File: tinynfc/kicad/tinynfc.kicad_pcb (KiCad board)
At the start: 2 copper layers, 40 x 40 mm, 15 parts, among them Q1 Diodes_DFN1006-3, U1 NXP_SOT902-3_XQFN8, U2 VQFN-20-1EP_3x3mm_P0.4mm_EP1.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

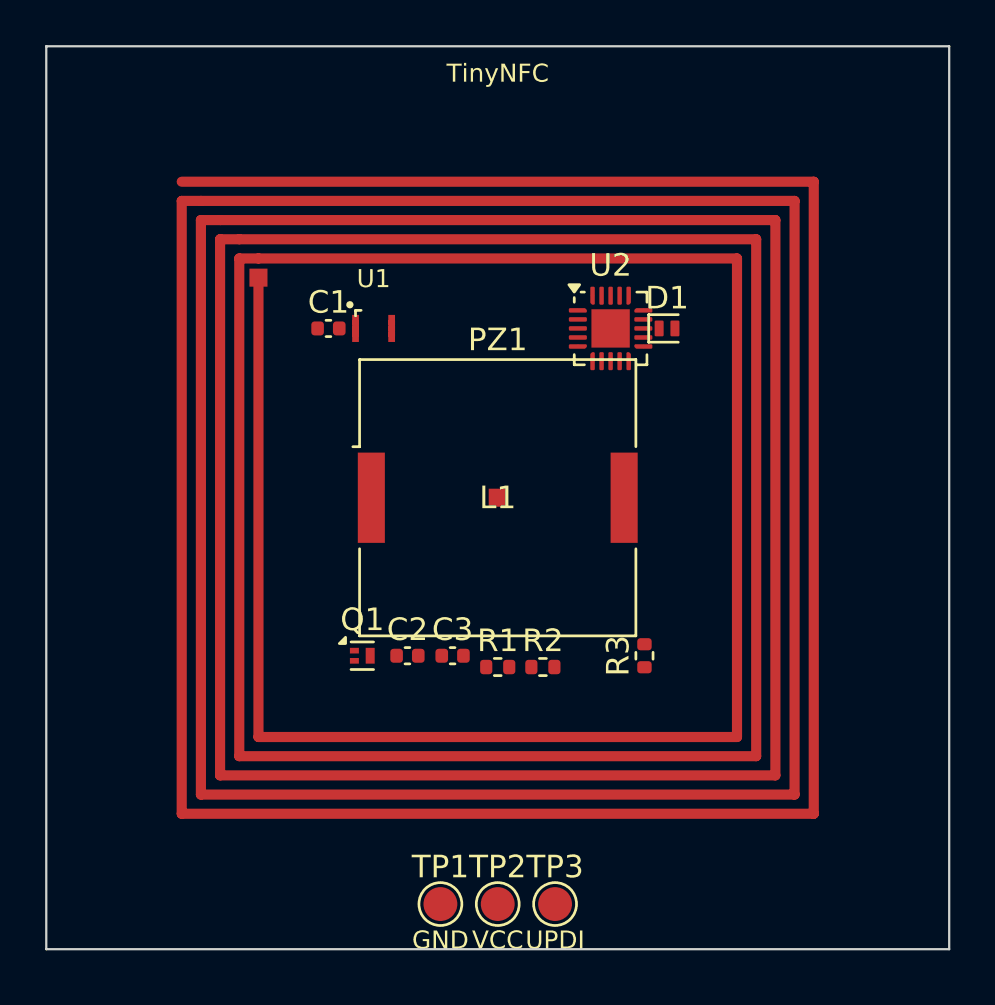
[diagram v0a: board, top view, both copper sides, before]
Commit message: Shrink TinyNFC to 28 mm postage stamp, not card size
Drop the outline from 40 mm to 28 mm with a 23 mm / 6-turn spiral, switch
to a 9×9 FUET-9018 piezo so the island fits, hide footprint silk refs that
were landing on copper, and refresh BOM/design costs for the smaller board.

Co-authored-by: Jason Hall <imjasonh@users.noreply.github.com>
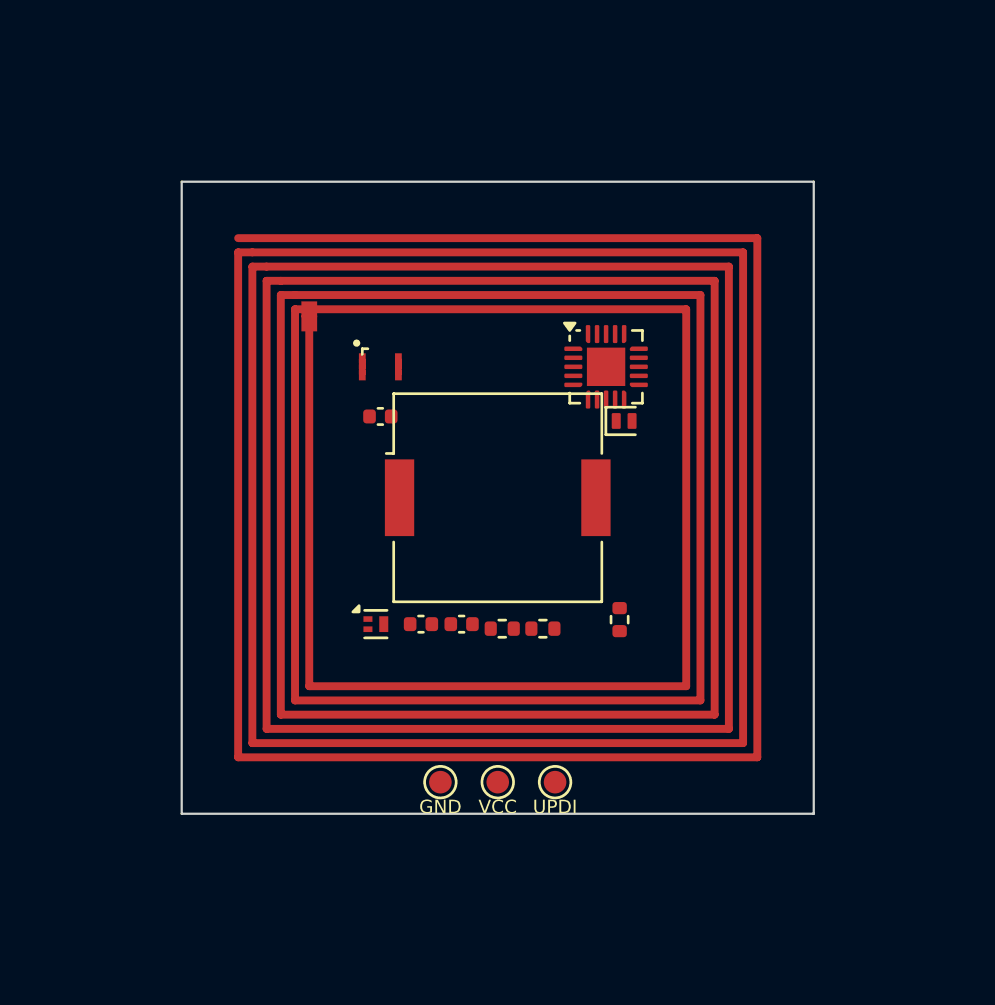
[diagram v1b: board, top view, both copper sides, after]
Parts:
- PZ1: value Buzzer_Murata_PKLCS1212E -> Buzzer_Murata_PKMCS0909E; footprint Buzzer_Murata_PKLCS1212E -> Buzzer_Murata_PKMCS0909E
- TP1, TP2, TP3: value TestPoint_Pad_D1.5mm -> TestPoint_Pad_D1.0mm; footprint TestPoint_Pad_D1.5mm -> TestPoint_Pad_D1.0mm
- moved TP1 5.40 mm to (-2.54, 12.6)
- moved TP2 5.40 mm to (0.00, 12.6)
- moved TP3 5.40 mm to (2.54, 12.6)
- moved C1 4.53 mm to (-5.20, -3.60)
- moved D1 4.52 mm to (5.60, -3.40)
- moved R3 1.94 mm to (5.40, 5.40)
- moved U1 1.73 mm to (-5.20, -5.80)
- moved R1 1.71 mm to (0.20, 5.80)
- moved U2 1.71 mm to (4.80, -5.80)
- moved R2 1.70 mm to (2.00, 5.80)
- moved C2 1.52 mm to (-3.40, 5.60)
- moved Q1 1.52 mm to (-5.40, 5.60)
- moved C3 1.46 mm to (-1.60, 5.60)
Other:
- board size 40 x 40 mm -> 28 x 28 mm
- board text removed: "TinyNFC"

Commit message: Add BOM qty breaks and US-quarter scale on TinyNFC PCB
Price 10 / 50 / 100 assembled runs in BOM.md, document 1.6 mm FR-4
(~3.4 mm assembled) thickness, and draw a Dwgs.User quarter outline
beside the 28 mm board for scale.

Co-authored-by: Jason Hall <imjasonh@users.noreply.github.com>
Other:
- board text added: "US quarter"
- board text added: "assembled ~3.4 mm tall"
- board text added: "board 28×28×1.6 mm"
- board text added: "Ø24.26 mm"

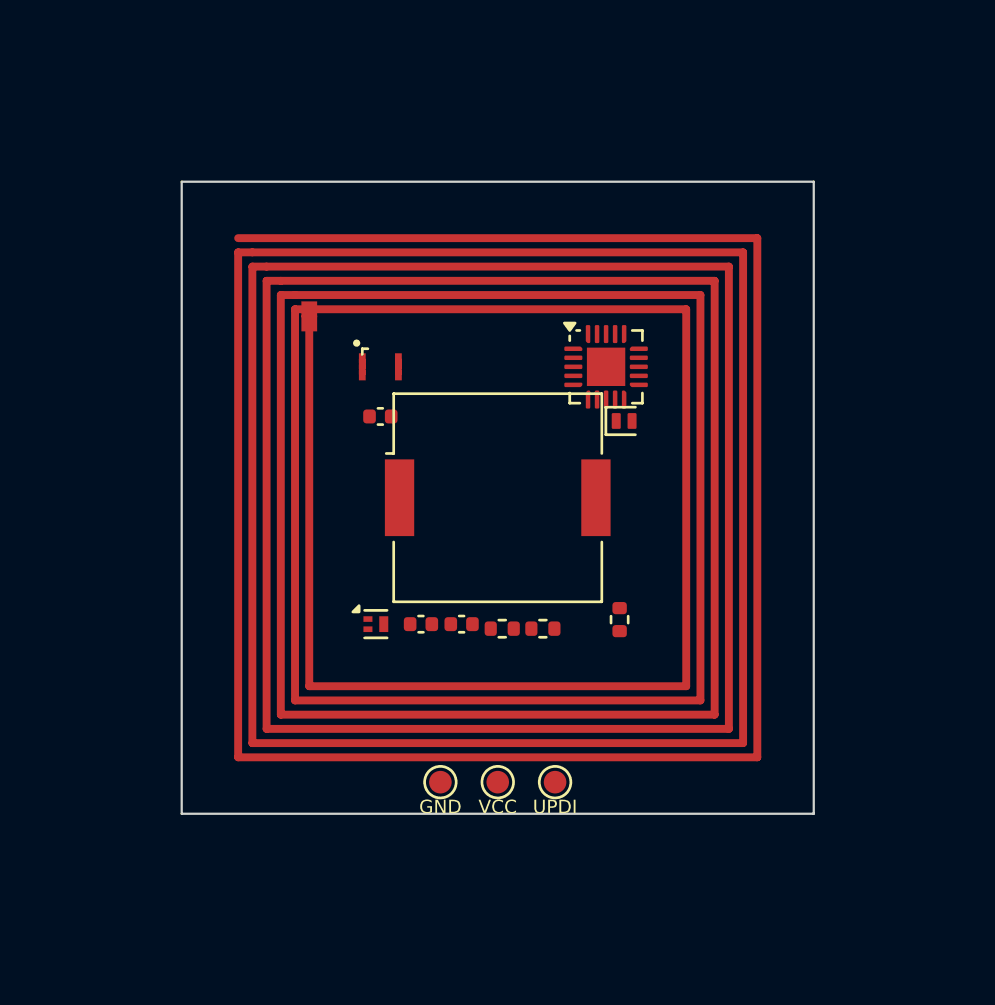
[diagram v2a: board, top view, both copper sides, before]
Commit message: Make TinyNFC board and antenna circular
Switch the Edge.Cuts outline to Ø 28 mm and replace the square spiral with
a Ø 24 mm Archimedean spiral so the coil matches phone NFC geometry better.
Update design, BOM, and README for the round postage-stamp disc.

Co-authored-by: Jason Hall <imjasonh@users.noreply.github.com>
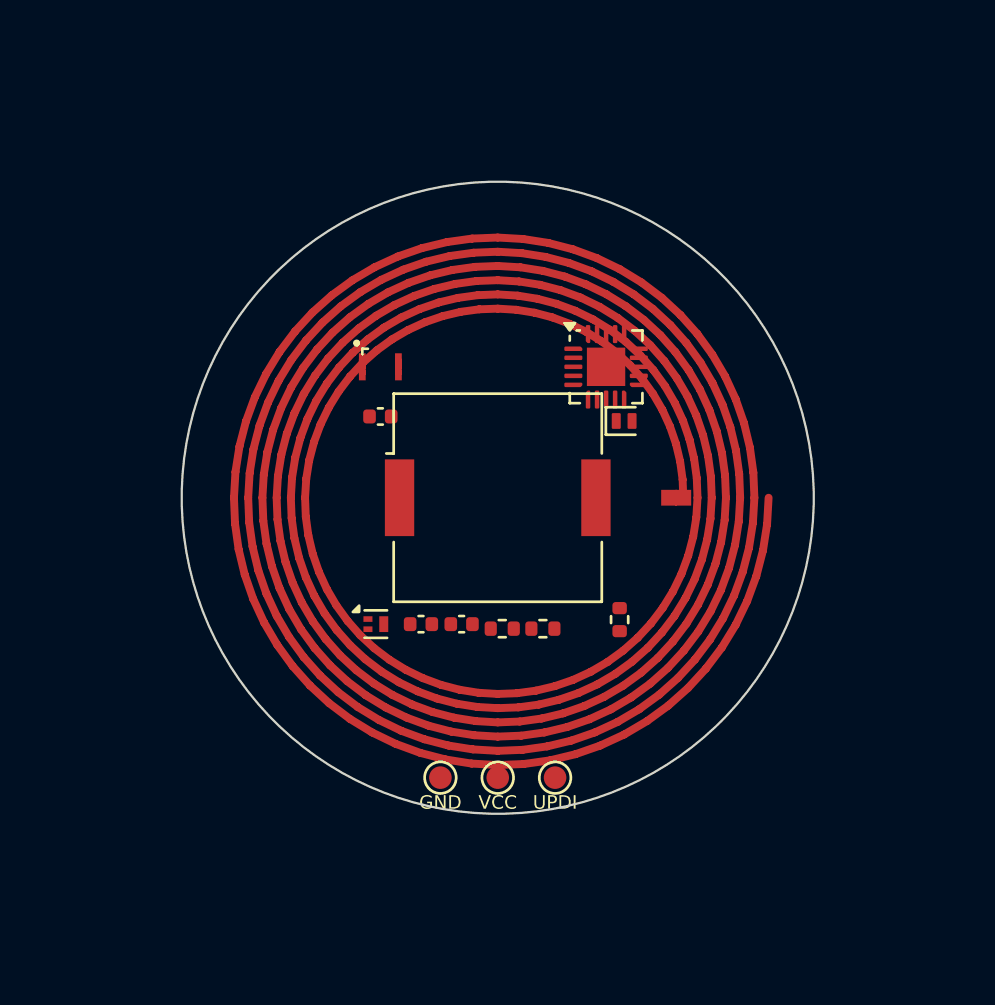
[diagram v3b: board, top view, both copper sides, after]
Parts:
- L1: value PCB_Antenna_RectSpiral -> PCB_Antenna_RoundSpiral; footprint PCB_Antenna_RectSpiral -> PCB_Antenna_RoundSpiral
- moved TP1 0.20 mm to (-2.54, 12.4)
- moved TP2 0.20 mm to (0.00, 12.4)
- moved TP3 0.20 mm to (2.54, 12.4)
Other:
- outline, holes or cut-outs redrawn
- board text added: "board Ø28×1.6 mm"
- board text removed: "board 28×28×1.6 mm"

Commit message: Keep TinyNFC parts clear of the circular spiral
Shift the piezo north and pack the ATtiny, NT3H, passives, and UPDI
pads into the south island. Stop the spiral at an inner clear radius,
move feeds to the west rim, and fail generation on pad/antenna or
pad/pad overlaps.

Co-authored-by: Jason Hall <imjasonh@users.noreply.github.com>
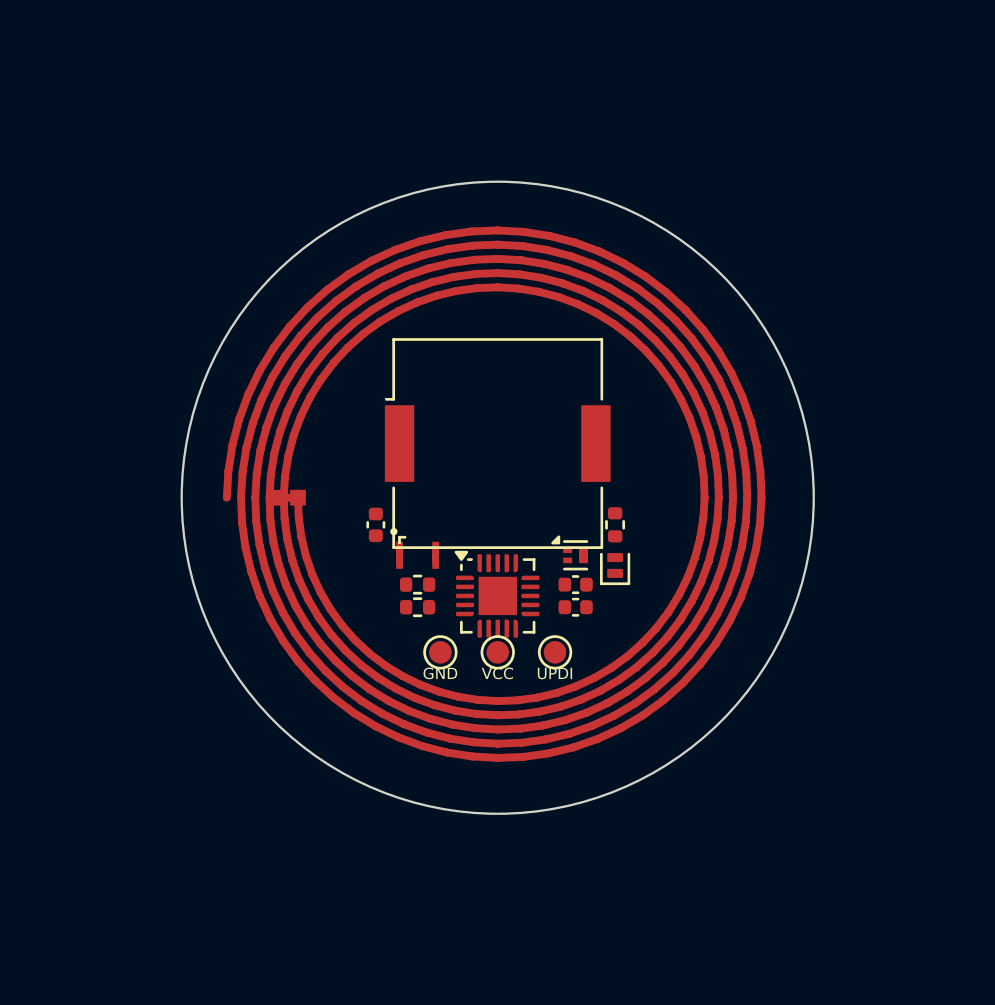
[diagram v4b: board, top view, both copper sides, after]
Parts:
- moved U2 11.2 mm to (0.00, 4.35)
- moved Q1 9.36 mm to (3.45, 2.55)
- moved U1 8.51 mm to (-3.55, 2.55)
- moved C2 7.07 mm to (3.45, 3.85)
- moved D1 6.41 mm to (5.20, 3.00), turned to 90 degrees
- moved R2 5.63 mm to (-3.55, 4.85)
- moved TP1 5.55 mm to (-2.54, 6.85)
- moved TP2 5.55 mm to (0.00, 6.85)
- moved TP3 5.55 mm to (2.54, 6.85)
- moved C3 5.11 mm to (3.45, 4.85)
- moved C1 4.80 mm to (-5.40, 1.20), turned to 90 degrees
- moved R1 4.23 mm to (-3.55, 3.85)
- moved R3 4.20 mm to (5.20, 1.20)
- moved PZ1 2.40 mm to (0.00, -2.40)

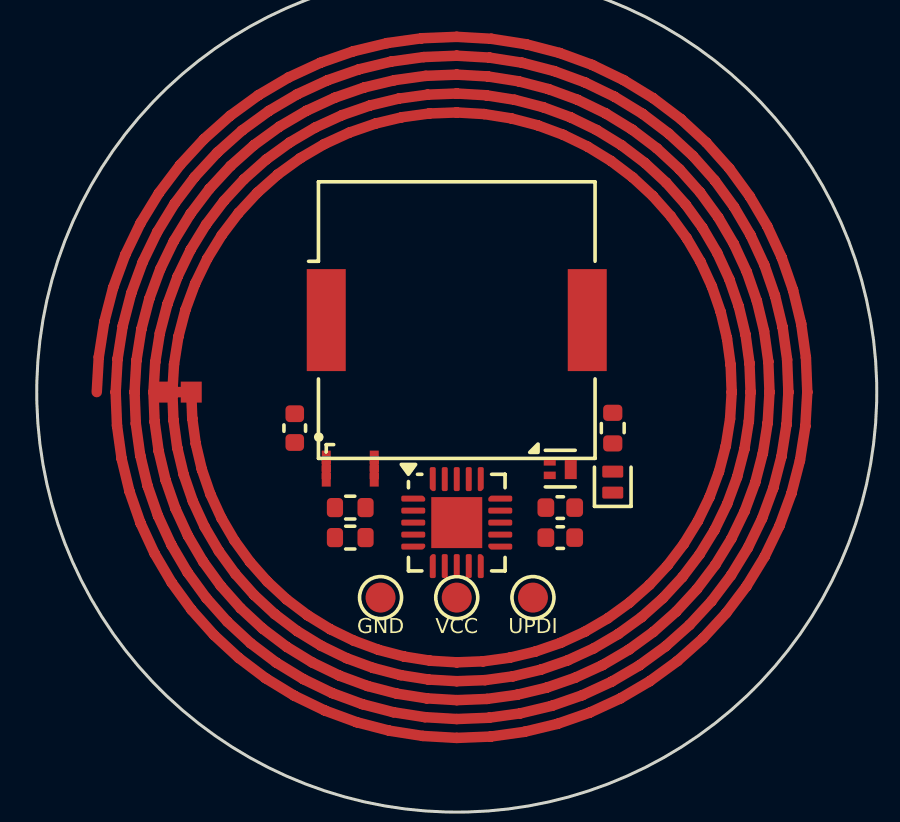
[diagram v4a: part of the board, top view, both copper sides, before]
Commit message: Spread TinyNFC parts into piezo east/west flanks
Put the antenna tune and VOUT bypass caps in the NW/NE pockets beside
the piezo, keep the NT3H and power chain on the side columns, and leave
the ATtiny plus UPDI pads on the south rim.

Co-authored-by: Jason Hall <imjasonh@users.noreply.github.com>
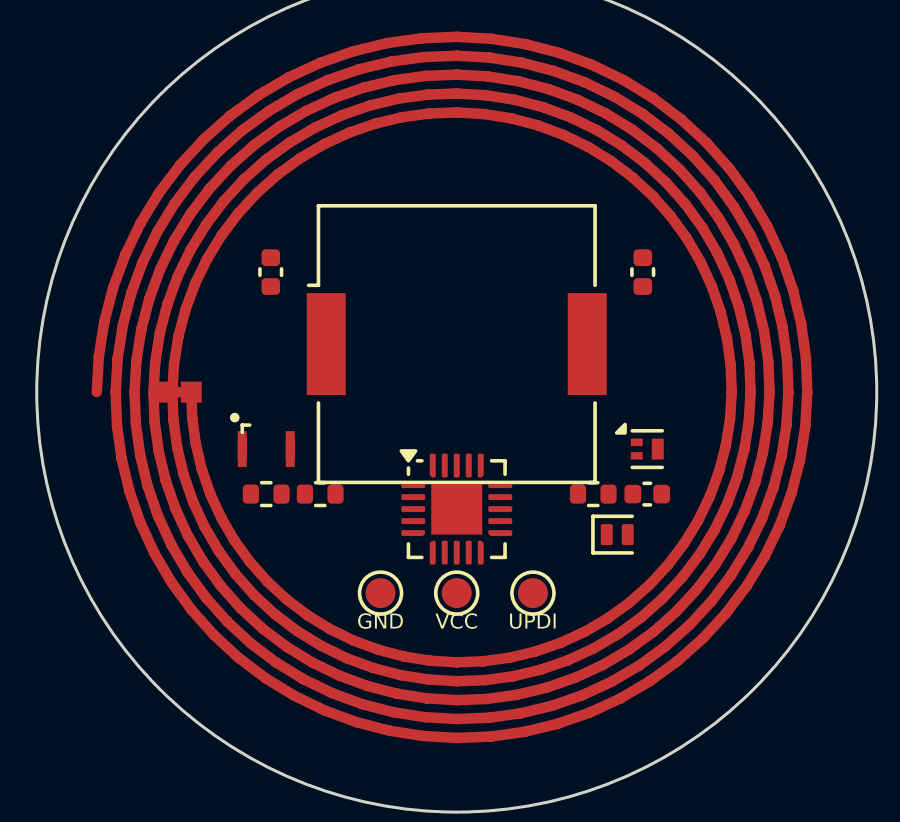
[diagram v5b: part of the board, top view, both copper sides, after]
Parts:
- moved C2 8.32 mm to (6.20, -4.00), turned to 90 degrees
- moved C1 5.26 mm to (-6.20, -4.00)
- moved C3 3.24 mm to (6.35, 3.40)
- moved Q1 2.97 mm to (6.35, 1.90)
- moved U1 2.87 mm to (-6.35, 1.90)
- moved R1 2.84 mm to (-6.35, 3.40)
- moved R3 2.29 mm to (4.55, 3.40), turned to 0 degrees
- moved R2 1.76 mm to (-4.55, 3.40)
- moved D1 1.76 mm to (5.35, 4.75), turned to 0 degrees
- moved PZ1 0.80 mm to (0.00, -1.60)
- moved U2 0.45 mm to (0.00, 3.90)
- moved TP1 0.15 mm to (-2.54, 6.70)
- moved TP2 0.15 mm to (0.00, 6.70)
- moved TP3 0.15 mm to (2.54, 6.70)

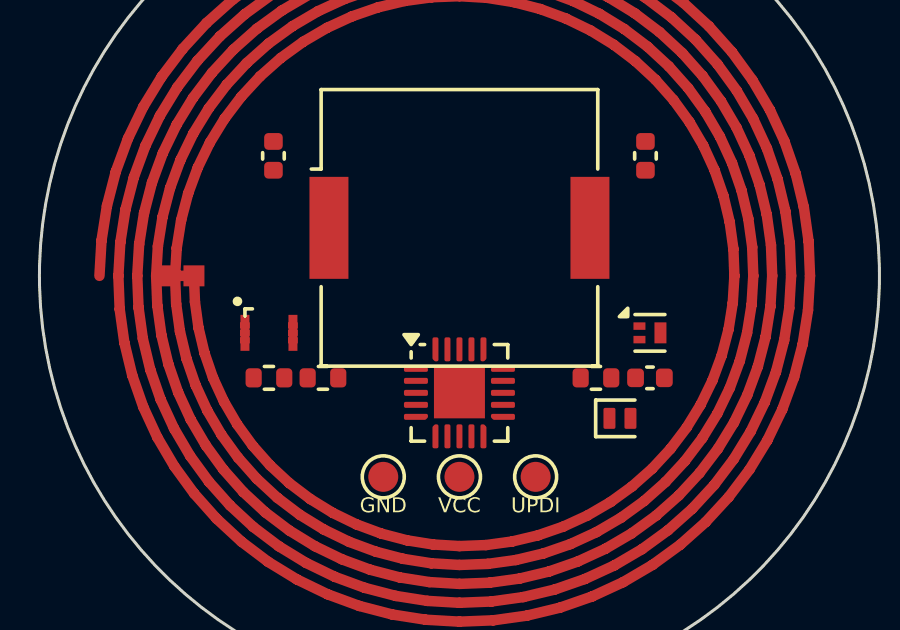
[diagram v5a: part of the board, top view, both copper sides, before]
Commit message: Place NT3H and P-FET beside the TinyNFC piezo
Sit U1/Q1 level with the piezo in the east/west flanks, keep tune/bypass
caps in the NW/NE pockets, and leave the ATtiny with UPDI on the south rim.

Co-authored-by: Jason Hall <imjasonh@users.noreply.github.com>
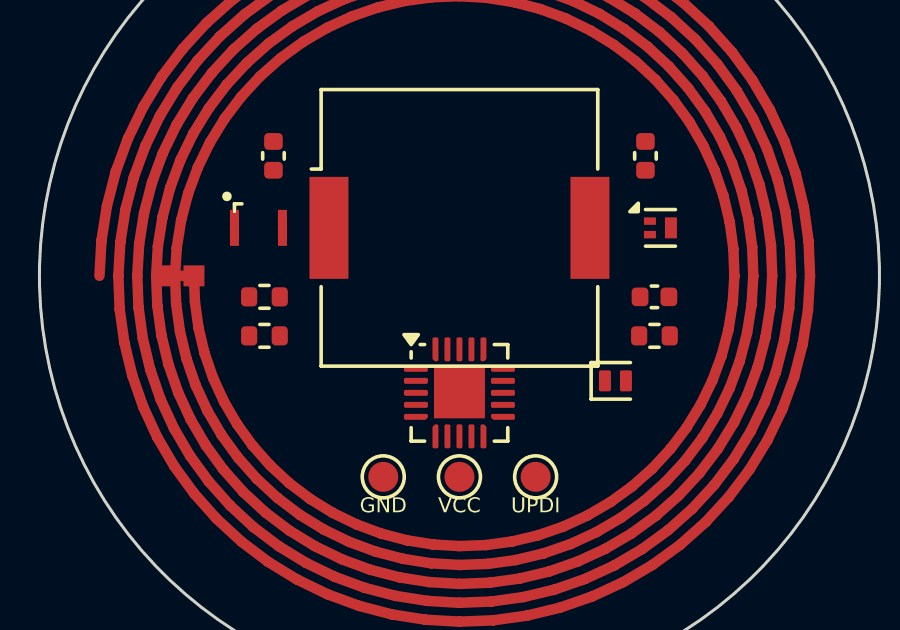
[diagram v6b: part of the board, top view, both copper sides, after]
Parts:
- moved Q1 3.52 mm to (6.70, -1.60)
- moved U1 3.52 mm to (-6.70, -1.60)
- moved C3 2.70 mm to (6.50, 0.70)
- moved R1 2.70 mm to (-6.50, 0.70)
- moved R2 2.40 mm to (-6.50, 2.00)
- moved R3 2.40 mm to (6.50, 2.00)
- moved D1 1.26 mm to (5.20, 3.50)
